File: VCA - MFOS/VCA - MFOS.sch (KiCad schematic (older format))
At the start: 77 parts

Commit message: added component list and datasheets uwu
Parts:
- removed J? (x8): AudioJack2, symbol Connector:AudioJack2
- added J? (x8): Conn_01x01_Female, symbol Connector:Conn_01x01_Female
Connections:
- net at R?.2: now also J?.1 (Pin_1) (x6)
- net at R?.1: now also J?.1 (Pin_1) (x2)
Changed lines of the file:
@@
 EESchema Schematic File Version 4
+LIBS:VCA - MFOS-cache
 EELAYER 29 0
 EELAYER END
@@
 $EndDescr
 $Comp
-L Connector:AudioJack2 J?
-U 1 1 5FCA5885
-P 1000 1100
-F 0 "J?" H 821 1083 50  0000 R CNN
-F 1 "AudioJack2" H 821 1174 50  0000 R CNN
-F 2 "" H 1000 1100 50  0001 C CNN
-F 3 "~" H 1000 1100 50  0001 C CNN
-	1    1000 1100
-	1    0    0    1
-$EndComp
-$Comp
-L Connector:AudioJack2 J?
-U 1 1 5FCA6831
-P 1000 1750
-F 0 "J?" H 821 1733 50  0000 R CNN
-F 1 "AudioJack2" H 821 1824 50  0000 R CNN
-F 2 "" H 1000 1750 50  0001 C CNN
-F 3 "~" H 1000 1750 50  0001 C CNN
-	1    1000 1750
-	1    0    0    1
-$EndComp
-$Comp
-L Connector:AudioJack2 J?
-U 1 1 5FCA6A97
-P 1000 3550
-F 0 "J?" H 821 3533 50  0000 R CNN
-F 1 "AudioJack2" H 821 3624 50  0000 R CNN
-F 2 "" H 1000 3550 50  0001 C CNN
-F 3 "~" H 1000 3550 50  0001 C CNN
-	1    1000 3550
-	1    0    0    1
-$EndComp
-$Comp
-L Connector:AudioJack2 J?
-U 1 1 5FCA6CC2
-P 5450 3400
-F 0 "J?" H 5270 3383 50  0000 R CNN
-F 1 "AudioJack2" H 5270 3474 50  0000 R CNN
-F 2 "" H 5450 3400 50  0001 C CNN
-F 3 "~" H 5450 3400 50  0001 C CNN
-	1    5450 3400
-	-1   0    0    1
-$EndComp
-$Comp
 L Device:R_US R?
 U 1 1 5FCA72EE
@@
 	1    0    0    -1
 $EndComp
-$Comp
-L power:Earth #PWR?
-U 1 1 5FCDC05E
-P 1250 1250
-F 0 "#PWR?" H 1250 1000 50  0001 C CNN
-F 1 "Earth" H 1250 1100 50  0001 C CNN
-F 2 "" H 1250 1250 50  0001 C CNN
-F 3 "~" H 1250 1250 50  0001 C CNN
-	1    1250 1250
-	1    0    0    -1
-$EndComp
-$Comp
-L power:Earth #PWR?
-U 1 1 5FCDC8A8
-P 1250 1900
-F 0 "#PWR?" H 1250 1650 50  0001 C CNN
-F 1 "Earth" H 1250 1750 50  0001 C CNN
-F 2 "" H 1250 1900 50  0001 C CNN
-F 3 "~" H 1250 1900 50  0001 C CNN
-	1    1250 1900
-	1    0    0    -1
-$EndComp
-$Comp
-L power:Earth #PWR?
-U 1 1 5FCDD063
-P 1250 3700
-F 0 "#PWR?" H 1250 3450 50  0001 C CNN
-F 1 "Earth" H 1250 3550 50  0001 C CNN
-F 2 "" H 1250 3700 50  0001 C CNN
-F 3 "~" H 1250 3700 50  0001 C CNN
-	1    1250 3700
-	1    0    0    -1
-$EndComp
-$Comp
-L power:Earth #PWR?
-U 1 1 5FCDD761
-P 5200 3550
-F 0 "#PWR?" H 5200 3300 50  0001 C CNN
-F 1 "Earth" H 5200 3400 50  0001 C CNN
-F 2 "" H 5200 3550 50  0001 C CNN
-F 3 "~" H 5200 3550 50  0001 C CNN
-	1    5200 3550
-	1    0    0    -1
-$EndComp
-Wire Wire Line
-	1250 1250 1250 1200
-Wire Wire Line
-	1250 1200 1200 1200
 Wire Wire Line
 	1300 1100 1200 1100
-Wire Wire Line
-	1250 1900 1250 1850
-Wire Wire Line
-	1250 1850 1200 1850
 Wire Wire Line
 	1300 1750 1200 1750
@@
 	4800 2250 4700 2250
 Wire Wire Line
-	1250 3700 1250 3650
-Wire Wire Line
-	1250 3650 1200 3650
-Wire Wire Line
 	1300 3550 1200 3550
 Wire Wire Line
@@
 Wire Wire Line
 	5250 3400 5100 3400
-Wire Wire Line
-	5200 3550 5200 3500
-Wire Wire Line
-	5200 3500 5250 3500
 $Comp
 L Device:R_US R?
@@
 Wire Wire Line
 	1300 6850 1300 7000
-$Comp
-L Connector:AudioJack2 J?
-U 1 1 5FEADD03
-P 6000 1500
-F 0 "J?" H 5821 1483 50  0000 R CNN
-F 1 "AudioJack2" H 5821 1574 50  0000 R CNN
-F 2 "" H 6000 1500 50  0001 C CNN
-F 3 "~" H 6000 1500 50  0001 C CNN
-	1    6000 1500
-	1    0    0    1
-$EndComp
-$Comp
-L Connector:AudioJack2 J?
-U 1 1 5FEADD09
-P 6000 2150
-F 0 "J?" H 5821 2133 50  0000 R CNN
-F 1 "AudioJack2" H 5821 2224 50  0000 R CNN
-F 2 "" H 6000 2150 50  0001 C CNN
-F 3 "~" H 6000 2150 50  0001 C CNN
-	1    6000 2150
-	1    0    0    1
-$EndComp
-$Comp
-L Connector:AudioJack2 J?
-U 1 1 5FEADD0F
-P 6000 3950
-F 0 "J?" H 5821 3933 50  0000 R CNN
-F 1 "AudioJack2" H 5821 4024 50  0000 R CNN
-F 2 "" H 6000 3950 50  0001 C CNN
-F 3 "~" H 6000 3950 50  0001 C CNN
-	1    6000 3950
-	1    0    0    1
-$EndComp
-$Comp
-L Connector:AudioJack2 J?
-U 1 1 5FEADD15
-P 10450 3800
-F 0 "J?" H 10270 3783 50  0000 R CNN
-F 1 "AudioJack2" H 10270 3874 50  0000 R CNN
-F 2 "" H 10450 3800 50  0001 C CNN
-F 3 "~" H 10450 3800 50  0001 C CNN
-	1    10450 3800
-	-1   0    0    1
-$EndComp
 $Comp
 L Device:R_US R?
@@
 	1    0    0    -1
 $EndComp
-$Comp
-L power:Earth #PWR?
-U 1 1 5FEADE29
-P 6250 1650
-F 0 "#PWR?" H 6250 1400 50  0001 C CNN
-F 1 "Earth" H 6250 1500 50  0001 C CNN
-F 2 "" H 6250 1650 50  0001 C CNN
-F 3 "~" H 6250 1650 50  0001 C CNN
-	1    6250 1650
-	1    0    0    -1
-$EndComp
-$Comp
-L power:Earth #PWR?
-U 1 1 5FEADE2F
-P 6250 2300
-F 0 "#PWR?" H 6250 2050 50  0001 C CNN
-F 1 "Earth" H 6250 2150 50  0001 C CNN
-F 2 "" H 6250 2300 50  0001 C CNN
-F 3 "~" H 6250 2300 50  0001 C CNN
-	1    6250 2300
-	1    0    0    -1
-$EndComp
-$Comp
-L power:Earth #PWR?
-U 1 1 5FEADE35
-P 6250 4100
-F 0 "#PWR?" H 6250 3850 50  0001 C CNN
-F 1 "Earth" H 6250 3950 50  0001 C CNN
-F 2 "" H 6250 4100 50  0001 C CNN
-F 3 "~" H 6250 4100 50  0001 C CNN
-	1    6250 4100
-	1    0    0    -1
-$EndComp
-$Comp
-L power:Earth #PWR?
-U 1 1 5FEADE3B
-P 10200 3950
-F 0 "#PWR?" H 10200 3700 50  0001 C CNN
-F 1 "Earth" H 10200 3800 50  0001 C CNN
-F 2 "" H 10200 3950 50  0001 C CNN
-F 3 "~" H 10200 3950 50  0001 C CNN
-	1    10200 3950
-	1    0    0    -1
-$EndComp
-Wire Wire Line
-	6250 1650 6250 1600
-Wire Wire Line
-	6250 1600 6200 1600
 Wire Wire Line
 	6300 1500 6200 1500
-Wire Wire Line
-	6250 2300 6250 2250
-Wire Wire Line
-	6250 2250 6200 2250
 Wire Wire Line
 	6300 2150 6200 2150
@@
 Wire Wire Line
 	9800 2650 9700 2650
-Wire Wire Line
-	6250 4100 6250 4050
-Wire Wire Line
-	6250 4050 6200 4050
 Wire Wire Line
 	6300 3950 6200 3950
@@
 Wire Wire Line
 	9050 5000 9050 4700
-Wire Wire Line
-	10250 3800 10100 3800
-Wire Wire Line
-	10200 3950 10200 3900
-Wire Wire Line
-	10200 3900 10250 3900
 $Comp
 L Device:R_US R?
@@
 	8450 4150 8450 4350
 Connection ~ 9050 4350
+$Comp
+L Connector:Conn_01x01_Female J?
+U 1 1 5FF31830
+P 1000 1100
+F 0 "J?" H 892 1285 50  0000 C CNN
+F 1 "Conn_01x01_Female" H 892 1194 50  0000 C CNN
+F 2 "" H 1000 1100 50  0001 C CNN
+F 3 "~" H 1000 1100 50  0001 C CNN
+	1    1000 1100
+	-1   0    0    -1
+$EndComp
+$Comp
+L Connector:Conn_01x01_Female J?
+U 1 1 5FF7F45B
+P 1000 1750
+F 0 "J?" H 892 1935 50  0000 C CNN
+F 1 "Conn_01x01_Female" H 892 1844 50  0000 C CNN
+F 2 "" H 1000 1750 50  0001 C CNN
+F 3 "~" H 1000 1750 50  0001 C CNN
+	1    1000 1750
+	-1   0    0    -1
+$EndComp
+$Comp
+L Connector:Conn_01x01_Female J?
+U 1 1 5FF910DC
+P 1000 3550
+F 0 "J?" H 892 3735 50  0000 C CNN
+F 1 "Conn_01x01_Female" H 892 3644 50  0000 C CNN
+F 2 "" H 1000 3550 50  0001 C CNN
+F 3 "~" H 1000 3550 50  0001 C CNN
+	1    1000 3550
+	-1   0    0    -1
+$EndComp
+$Comp
+L Connector:Conn_01x01_Female J?
+U 1 1 5FF9182F
+P 5450 3400
+F 0 "J?" H 5478 3426 50  0000 L CNN
+F 1 "Conn_01x01_Female" H 5478 3335 50  0000 L CNN
+F 2 "" H 5450 3400 50  0001 C CNN
+F 3 "~" H 5450 3400 50  0001 C CNN
+	1    5450 3400
+	1    0    0    -1
+$EndComp
+$Comp
+L Connector:Conn_01x01_Female J?
+U 1 1 5FF9A8C7
+P 6000 3950
+F 0 "J?" H 5892 4135 50  0000 C CNN
+F 1 "Conn_01x01_Female" H 5892 4044 50  0000 C CNN
+F 2 "" H 6000 3950 50  0001 C CNN
+F 3 "~" H 6000 3950 50  0001 C CNN
+	1    6000 3950
+	-1   0    0    -1
+$EndComp
+$Comp
+L Connector:Conn_01x01_Female J?
+U 1 1 5FFBC46A
+P 6000 2150
+F 0 "J?" H 5892 2335 50  0000 C CNN
+F 1 "Conn_01x01_Female" H 5892 2244 50  0000 C CNN
+F 2 "" H 6000 2150 50  0001 C CNN
+F 3 "~" H 6000 2150 50  0001 C CNN
+	1    6000 2150
+	-1   0    0    -1
+$EndComp
+$Comp
+L Connector:Conn_01x01_Female J?
+U 1 1 5FFBCC11
+P 6000 1500
+F 0 "J?" H 5892 1685 50  0000 C CNN
+F 1 "Conn_01x01_Female" H 5892 1594 50  0000 C CNN
+F 2 "" H 6000 1500 50  0001 C CNN
+F 3 "~" H 6000 1500 50  0001 C CNN
+	1    6000 1500
+	-1   0    0    -1
+$EndComp
+Wire Wire Line
+	10250 3800 10100 3800
+$Comp
+L Connector:Conn_01x01_Female J?
+U 1 1 5FFBD007
+P 10450 3800
+F 0 "J?" H 10478 3826 50  0000 L CNN
+F 1 "Conn_01x01_Female" H 10478 3735 50  0000 L CNN
+F 2 "" H 10450 3800 50  0001 C CNN
+F 3 "~" H 10450 3800 50  0001 C CNN
+	1    10450 3800
+	1    0    0    -1
+$EndComp
 $EndSCHEMATC

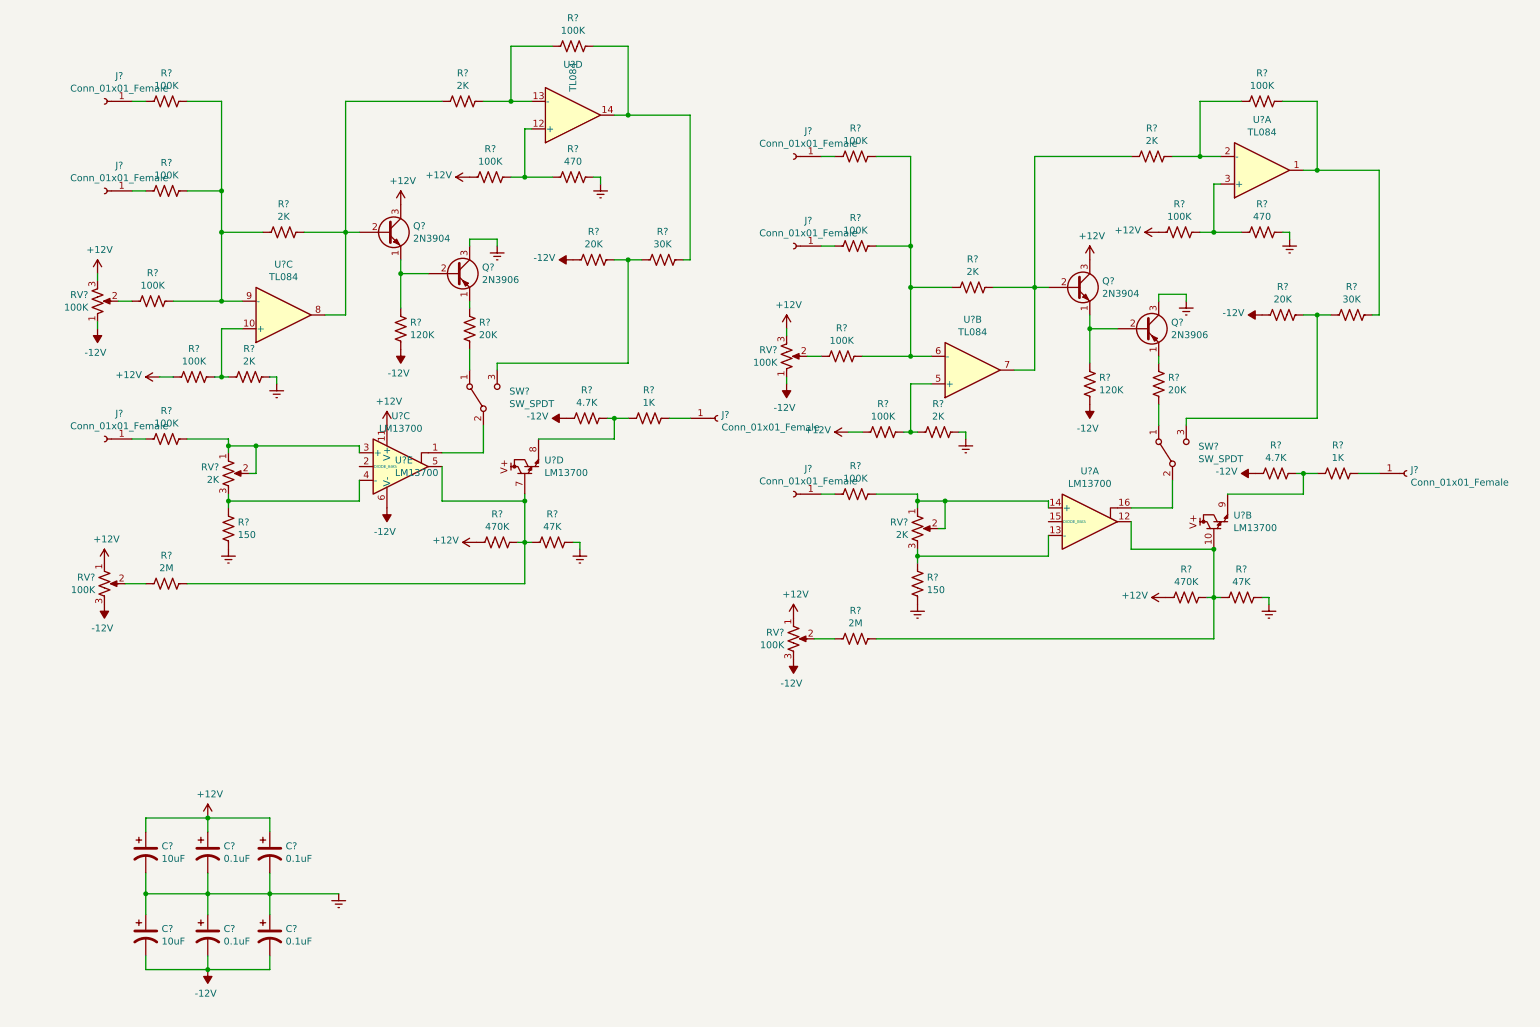
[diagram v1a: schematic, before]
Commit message: datasheets for 2N3906 and 2N3904 added
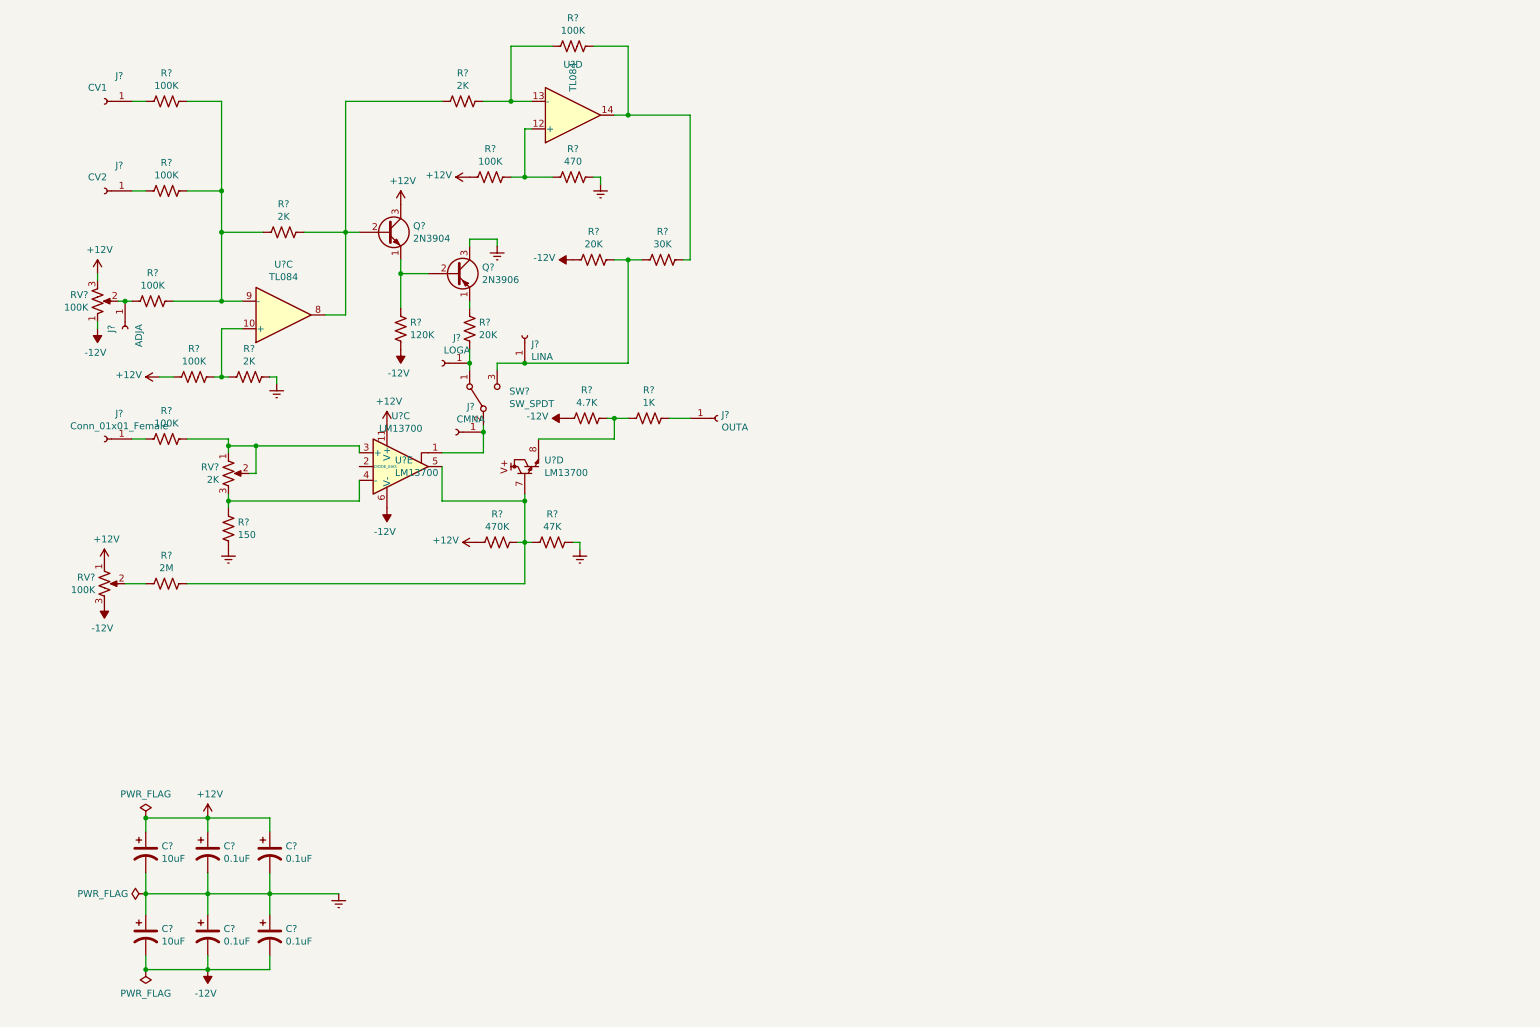
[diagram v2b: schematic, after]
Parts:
- removed J? (x4): Conn_01x01_Female, symbol Connector:Conn_01x01_Female
- removed Q?: 2N3904, Package_TO_SOT_THT:TO-92_Inline, symbol Transistor_BJT:2N3904
- removed Q?: 2N3906, Package_TO_SOT_THT:TO-92_Inline, symbol Transistor_BJT:2N3906
- removed R? (x7): 100K, symbol Device:R_US
- removed R? (x3): 2K, symbol Device:R_US
- removed R?: 120K, symbol Device:R_US
- removed R? (x2): 20K, symbol Device:R_US
- removed R?: 1K, symbol Device:R_US
- removed R?: 470, symbol Device:R_US
- removed R?: 30K, symbol Device:R_US
- removed R?: 2M, symbol Device:R_US
- removed R?: 150, symbol Device:R_US
- removed R?: 470K, symbol Device:R_US
- removed R?: 47K, symbol Device:R_US
- removed R?: 4.7K, symbol Device:R_US
- removed RV? (x2): 100K, symbol Device:R_POT_US
- removed RV?: 2K, symbol Device:R_POT_US
- removed SW?: SW_SPDT, symbol Switch:SW_SPDT
- removed U? (x2): TL084, symbol Amplifier_Operational:TL084
- removed U? (x2): LM13700, symbol Amplifier_Operational:LM13700
- added J?: ADJA, symbol Connector:Conn_01x01_Female
- added J?: LOGA, symbol Connector:Conn_01x01_Female
- added J?: LINA, symbol Connector:Conn_01x01_Female
- added J?: CMNA, symbol Connector:Conn_01x01_Female
- J?: value Conn_01x01_Female -> CV1
- J?: value Conn_01x01_Female -> CV2
- J?: value Conn_01x01_Female -> OUTA
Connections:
- net at R?.2, RV?.2: now also J?.1 (Pin_1)
- net at R?.2, SW?.1 (A): now also J?.1 (Pin_1)
- net at SW?.2 (B), U?.1: now also J?.1 (Pin_1)
- net at R?.1, R?.2, SW?.3 (C): now also J?.1 (Pin_1)

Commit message: more sheetzp-0o
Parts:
- added J10: CVB2, Connector_Wire:SolderWirePad_1x01_Drill1mm, symbol Connector:Conn_01x01_Female
- added J11: Sig_In_B, Connector_Wire:SolderWirePad_1x01_Drill1mm, symbol Connector:Conn_01x01_Female
- added J12: ADJA, Connector_Wire:SolderWirePad_1x01_Drill1mm, symbol Connector:Conn_01x01_Female
- added J13: LOGB, Connector_Wire:SolderWirePad_1x01_Drill1mm, symbol Connector:Conn_01x01_Female
- added J14: CMNB, Connector_Wire:SolderWirePad_1x01_Drill1mm, symbol Connector:Conn_01x01_Female
- added J15: LINB, Connector_Wire:SolderWirePad_1x01_Drill1mm, symbol Connector:Conn_01x01_Female
- added J16: OUTB, Connector_Wire:SolderWirePad_1x01_Drill1mm, symbol Connector:Conn_01x01_Female
- added J9: CVB1, Connector_Wire:SolderWirePad_1x01_Drill1mm, symbol Connector:Conn_01x01_Female
- added Q3: 2N3904, Package_TO_SOT_THT:TO-92_Inline_Wide, symbol Transistor_BJT:2N3904
- added Q4: 2N3906, Package_TO_SOT_THT:TO-92_Inline_Wide, symbol Transistor_BJT:2N3906
- added R22, R23, R24, R25, R27, R34, R37: 100K, Resistor_THT:R_Axial_DIN0207_L6.3mm_D2.5mm_P7.62mm_Horizontal, symbol Device:R_US
- added R26: 2M, Resistor_THT:R_Axial_DIN0207_L6.3mm_D2.5mm_P7.62mm_Horizontal, symbol Device:R_US
- added R28: 150, Resistor_THT:R_Axial_DIN0207_L6.3mm_D2.5mm_P7.62mm_Horizontal, symbol Device:R_US
- added R29, R30, R32: 2K, Resistor_THT:R_Axial_DIN0207_L6.3mm_D2.5mm_P7.62mm_Horizontal, symbol Device:R_US
- added R31: 120K, Resistor_THT:R_Axial_DIN0207_L6.3mm_D2.5mm_P7.62mm_Horizontal, symbol Device:R_US
- added R33, R40: 20K, Resistor_THT:R_Axial_DIN0207_L6.3mm_D2.5mm_P7.62mm_Horizontal, symbol Device:R_US
- added R35: 470K, Resistor_THT:R_Axial_DIN0207_L6.3mm_D2.5mm_P7.62mm_Horizontal, symbol Device:R_US
- added R36: 47K, Resistor_THT:R_Axial_DIN0207_L6.3mm_D2.5mm_P7.62mm_Horizontal, symbol Device:R_US
- added R38: 470, Resistor_THT:R_Axial_DIN0207_L6.3mm_D2.5mm_P7.62mm_Horizontal, symbol Device:R_US
- added R39: 4.7K, Resistor_THT:R_Axial_DIN0207_L6.3mm_D2.5mm_P7.62mm_Horizontal, symbol Device:R_US
- added R41: 1K, Resistor_THT:R_Axial_DIN0207_L6.3mm_D2.5mm_P7.62mm_Horizontal, symbol Device:R_US
- added R42: 30K, Resistor_THT:R_Axial_DIN0207_L6.3mm_D2.5mm_P7.62mm_Horizontal, symbol Device:R_US
- added RV4, RV5: 100K, symbol Device:R_POT_US
- added RV6: 2K, symbol Device:R_POT_US
- added SW2: LOG_SW_B, symbol Switch:SW_SPDT
- added U3: TL084, Package_DIP:DIP-14_W7.62mm_Socket, symbol Amplifier_Operational:TL084
- added U4: LM13700, Package_DIP:DIP-16_W7.62mm_Socket, symbol Amplifier_Operational:LM13700
- J1: renamed from J?; value CV1 -> CVA1; footprint (none) -> Connector_Wire:SolderWirePad_1x01_Drill1mm
- J2: renamed from J?; value CV2 -> CVA2; footprint (none) -> Connector_Wire:SolderWirePad_1x01_Drill1mm
- J3: renamed from J?; value Conn_01x01_Female -> Sig_In_A; footprint (none) -> Connector_Wire:SolderWirePad_1x01_Drill1mm
- J4, J5, J6, J7, J8: renamed from J?; footprint (none) -> Connector_Wire:SolderWirePad_1x01_Drill1mm
- Q1, Q2: renamed from Q?; footprint Package_TO_SOT_THT:TO-92_Inline -> Package_TO_SOT_THT:TO-92_Inline_Wide
- R1, R10, R11, R12, R13, R14, R15, R16, R17, R18, R19, R2, R20, R21, R3, R4, R5, R6, R7, R8, R9: renamed from R?; footprint (none) -> Resistor_THT:R_Axial_DIN0207_L6.3mm_D2.5mm_P7.62mm_Horizontal
- SW1: renamed from SW?; value SW_SPDT -> LOG_SW_A
- U1: renamed from U?; footprint (none) -> Package_DIP:DIP-14_W7.62mm_Socket
- U2: renamed from U?; footprint (none) -> Package_DIP:DIP-16_W7.62mm_Socket
- gave numbers to parts that had none: 9
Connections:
- net +12V: now also Q3.3 (C), R27.2, R34.2, R35.2, RV4.3, RV5.1, U4.11 (V+)
- net -12V: now also R31.2, R39.2, R40.2, RV4.1, RV5.3, U4.6 (V-)
- net Earth: now also Q4.3 (C), R28.2, R29.1, R36.1, R38.1
- new net: R22.1, R23.1, R24.1, R30.2, U3.9 (-)
- new net: J9.1 (Pin_1), R23.2
- new net: J10.1 (Pin_1), R24.2
- new net: J12.1 (Pin_1), R22.2, RV4.2
- new net: R27.1, R29.2, U3.10 (+)
- new net: Q3.2 (B), R30.1, R32.2, U3.8
- new net: Q3.1 (E), Q4.2 (B), R31.1
- new net: Q4.1 (E), R33.1
- new net: J13.1 (Pin_1), R33.2, SW2.1 (A)
- new net: J14.1 (Pin_1), SW2.2 (B), U4.1
- new net: J15.1 (Pin_1), R40.1, R42.2, SW2.3 (C)
- new net: R34.1, R38.2, U3.12 (+)
- new net: R32.1, R37.2, U3.13 (-)
- new net: R37.1, R42.1, U3.14
- new net: J16.1 (Pin_1), R41.1
- new net: R39.1, R41.2, U4.8
- new net: R25.1, RV6.1, RV6.2, U4.3 (+)
- new net: J11.1 (Pin_1), R25.2
- new net: R26.2, RV5.2
- new net: R26.1, R35.1, R36.2, U4.5, U4.7
- new net: R28.1, RV6.3, U4.4 (-)
- no-connect marks 0 -> 2
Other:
- moved on the sheet: J1, J2, J3, J4, J5, J6, J7, J8, Q1, Q2, R1, R10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

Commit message: finished schematic, placed and arranged parts on pcbnew
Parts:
- removed U3: TL084, Package_DIP:DIP-14_W7.62mm_Socket, symbol Amplifier_Operational:TL084
- removed U4: LM13700, Package_DIP:DIP-16_W7.62mm_Socket, symbol Amplifier_Operational:LM13700
- added J5: 12V_Conn, Connector_Wire:SolderWirePad_1x02_P3.81mm_Drill1mm, symbol Connector:Conn_01x01_Female
- added J6: -12V_Conn, Connector_Wire:SolderWirePad_1x02_P3.81mm_Drill1mm, symbol Connector:Conn_01x01_Female
- added J7: Gnd_Conn, Connector_Wire:SolderWirePad_1x02_P3.81mm_Drill1mm, symbol Connector:Conn_01x01_Female
- added unit 2 of U1
- added unit 1 of U1
- added unit 5 of U1
- added unit 1 of U2
- added unit 2 of U2
- C1, C2: footprint (none) -> Capacitor_THT:CP_Radial_D5.0mm_P2.50mm
- C3, C4, C5, C6: footprint (none) -> Capacitor_THT:C_Rect_L7.0mm_W2.5mm_P5.00mm
- J15: renamed from J12; value ADJA -> ADJB
- RV1: footprint (none) -> Connector_Wire:SolderWirePad_1x03_P4.445mm_Drill1.5mm
- RV2, RV3, RV5, RV6: footprint (none) -> Potentiometer_THT:Potentiometer_Runtron_RM-065_Vertical
- RV4: footprint (none) -> Connector_Wire:SolderWirePad_1x03_P3.175mm_Drill1mm
- SW1, SW2: footprint (none) -> Connector_Wire:SolderWirePad_1x03_P3.175mm_Drill0.8mm
- renumbered J7 to J10, J8 to J11, J9 to J12, J10 to J13, J11 to J14, J13 to J16, J14 to J17, J15 to J18, J16 to J19, J5 to J8, J6 to J9
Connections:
- net +12V: now also J5.1 (Pin_1), U1.4 (V+)
- net -12V: now also J6.1 (Pin_1), U1.11 (V-)
- net Earth: now also J7.1 (Pin_1)
- net at R22.1, R23.1, R24.1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: now also U1.6 (-)
- net at R27.1, R29.2: now also U1.5 (+)
- net at Q3.2 (B), R30.1, R32.2: now also U1.7
- net at J17.1 (Pin_1), SW2.2 (B): now also U2.16
- net at R34.1, R38.2: now also U1.3 (+)
- net at R32.1, R37.2: now also U1.2 (-)
- net at R37.1, R42.1: now also U1.1
- net at R39.1, R41.2: now also U2.9
- net at R25.1, RV6.1, RV6.2: now also U2.14 (+)
- net at R26.1, R35.1, R36.2: now also U2.10, U2.12
- net at R28.1, RV6.3: now also U2.13 (-)
